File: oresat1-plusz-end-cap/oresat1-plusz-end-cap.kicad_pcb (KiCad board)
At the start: 4 copper layers, 105.6 x 105.6 mm, 55 parts, among them J1 M55-7011242R, J2 U.FL-R-SMA, U1 RM3100, U2 RM3100

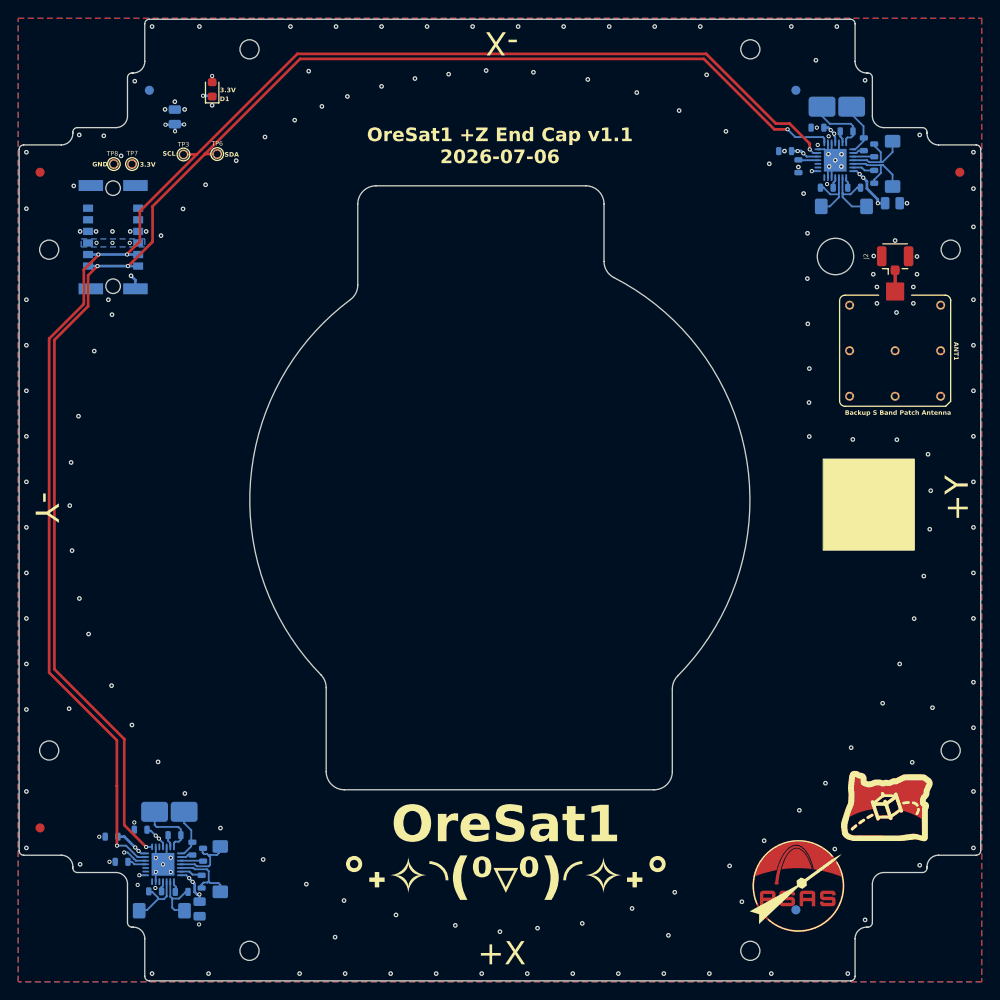
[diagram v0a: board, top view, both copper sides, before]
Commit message: Changes to layout
Aligned some magnetometer coils to align with axis of oresat 1
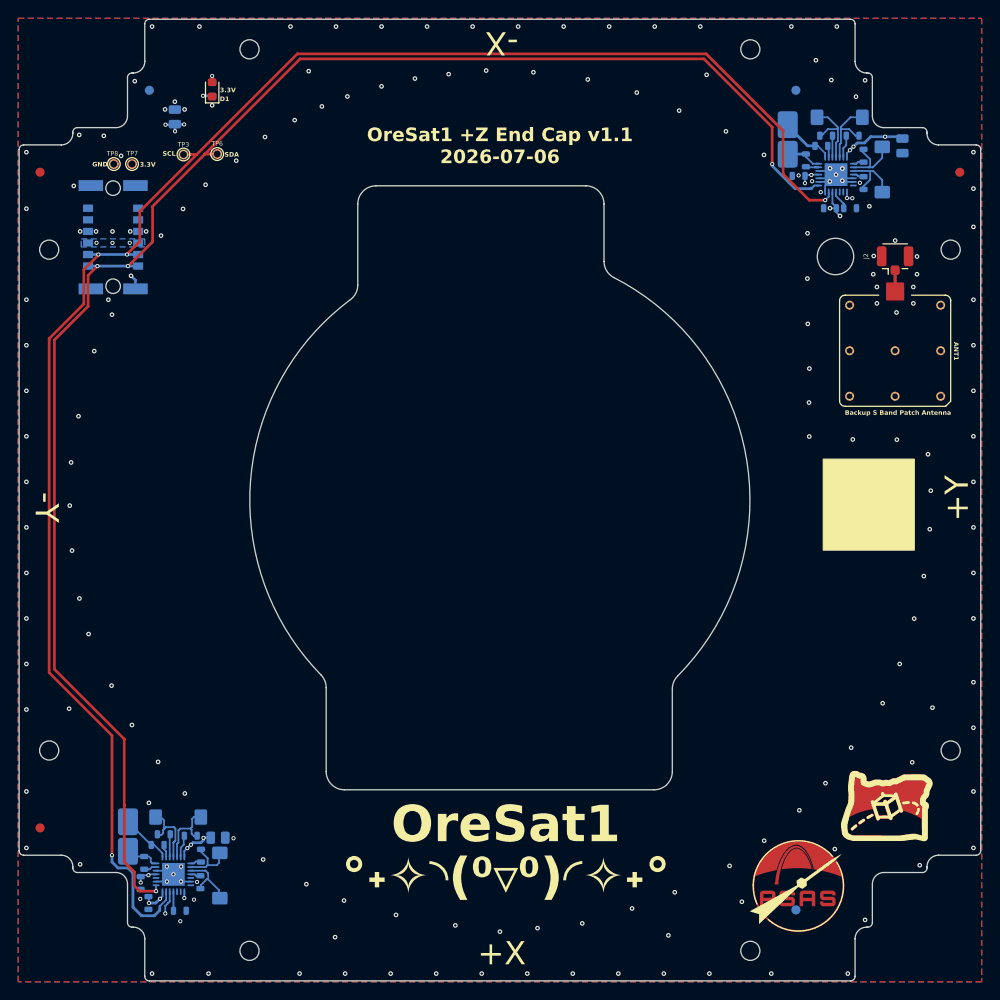
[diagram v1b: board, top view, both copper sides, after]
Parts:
- moved R9 8.36 mm to (113.3, 150.1), turned to 180 degrees
- moved C5 8.33 mm to (109.9, 149.2), turned to -90 degrees
- moved C3 8.07 mm to (117.5, 142.1), turned to 0 degrees
- moved C1 7.98 mm to (184.8, 73.0)
- moved L3 7.74 mm to (185.8, 63.0), turned to 180 degrees
- moved L7 7.45 mm to (117.7, 146.2), turned to 90 degrees
- moved L8 7.35 mm to (113.2, 139.8), turned to 180 degrees
- moved R8 7.31 mm to (186.9, 73.0), turned to 180 degrees
- moved L5 6.49 mm to (180.1, 65.4), turned to 90 degrees
- moved C2 6.40 mm to (192.7, 66.1), turned to -90 degrees
- moved C7 5.85 mm to (109.0, 147.1), turned to -90 degrees
- moved L4 5.84 mm to (190.5, 68.7), turned to 90 degrees
- moved C4 5.69 mm to (181.3, 69.4)
- moved R4 5.51 mm to (184.3, 65.0), turned to 0 degrees
- moved R6 5.49 mm to (182.1, 67.7), turned to -90 degrees
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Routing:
- net /MAG-SCL: track 172.7 -> 189.5 mm
- net /MAG-SDA: track 169.8 -> 180.0 mm
- net Net-(U2-ZINP): track 7.27 -> 4.44 mm
- net GND: track 18.2 -> 15.3 mm, vias 183 -> 178
- net Net-(U1-ZINP): track 6.63 -> 4.15 mm
- net +3.3v: track 30.2 -> 31.8 mm, vias 24 -> 27
- net Net-(U2-ZDRVP): track 1.30 -> 1.84 mm

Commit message: routine push
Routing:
- net Net-(U1-ZINP): track 4.15 -> 4.67 mm
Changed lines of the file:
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@@
+	)
+	(segment
+		(start 110.745 146.89)
+		(end 111.9225 146.89)
+		(width 0.2)
+		(layer "B.Cu")
+		(net "GND")
 	)
 	(segment
@@
 	)
 	(segment
-		(start 110.745 146.89)
-		(end 111.9225 146.89)
-		(width 0.2)
-		(layer "B.Cu")
-		(net "GND")
-	)
-	(segment
 		(start 114.55 146.9)
 		(end 113.4825 146.9)
@@
 	)
 	(segment
+		(start 110.3125 144.9)
+		(end 110.1525 144.74)
+		(width 0.2)
+		(layer "B.Cu")
+		(net "Net-(U1-ZINP)")
+	)
+	(segment
 		(start 109.44 144.14)
 		(end 108.215 144.14)
@@
 	)
 	(segment
+		(start 110.735 144.9)
+		(end 110.3125 144.9)
+		(width 0.2)
+		(layer "B.Cu")
+		(net "Net-(U1-ZINP)")
+	)
+	(segment
+		(start 109.9525 144.14)
+		(end 109.44 144.14)
+		(width 0.2)
+		(layer "B.Cu")
+		(net "Net-(U1-ZINP)")
+	)
+	(segment
 		(start 110.1525 144.34)
 		(end 109.9525 144.14)
@@
 	)
 	(segment
-		(start 110.3125 144.9)
-		(end 110.1525 144.74)
-		(width 0.2)
-		(layer "B.Cu")
-		(net "Net-(U1-ZINP)")
-	)
-	(segment
 		(start 108.215 144.14)
 		(end 107.65 143.575)
 		(width 0.2)
 		(layer "B.Cu")
-		(net "Net-(U1-ZINP)")
-	)
-	(segment
-		(start 110.735 144.9)
-		(end 110.3125 144.9)
-		(width 0.2)
-		(layer "B.Cu")

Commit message: routine push
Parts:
- added R16: 121, oresat-passives:0603-C-NOSILK, B.Cu at (117.8, 151.2)
- added R17: 121, oresat-passives:0603-C-NOSILK, B.Cu at (117.8, 150.1)
- added R18: 121, oresat-passives:0603-C-NOSILK, B.Cu at (115.6, 151.2)
- added R19: 121, oresat-passives:0603-C-NOSILK, B.Cu at (115.6, 150.1)
- moved R7 0.05 mm to (183.8, 66.1)
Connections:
- U1 pad 28: +3.3v -> Net-(U1-MISO/SA1)
- U1 pad 3: GND -> Net-(U1-SSN/SA0)
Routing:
- net Net-(U1-SSN/SA0): track 0.00 -> 9.65 mm, vias 0 -> 2
- net Net-(U1-MISO/SA1): track 0.00 -> 7.85 mm, vias 0 -> 2
- net +3.3v: track 31.8 -> 32.7 mm, vias 27 -> 24
- net GND: vias 178 -> 181

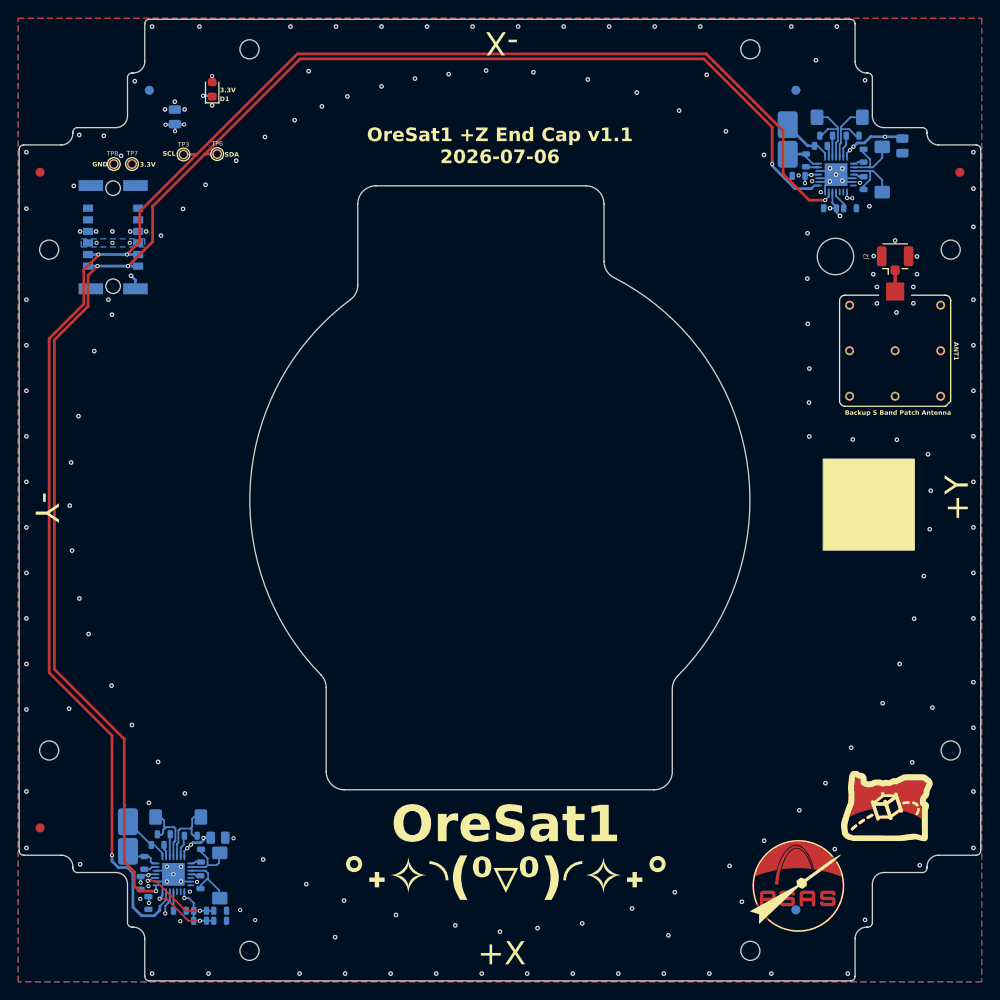
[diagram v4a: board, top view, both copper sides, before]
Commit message: Added releases, cleaned up PNI inductors, fixed ERCs and DRCs.
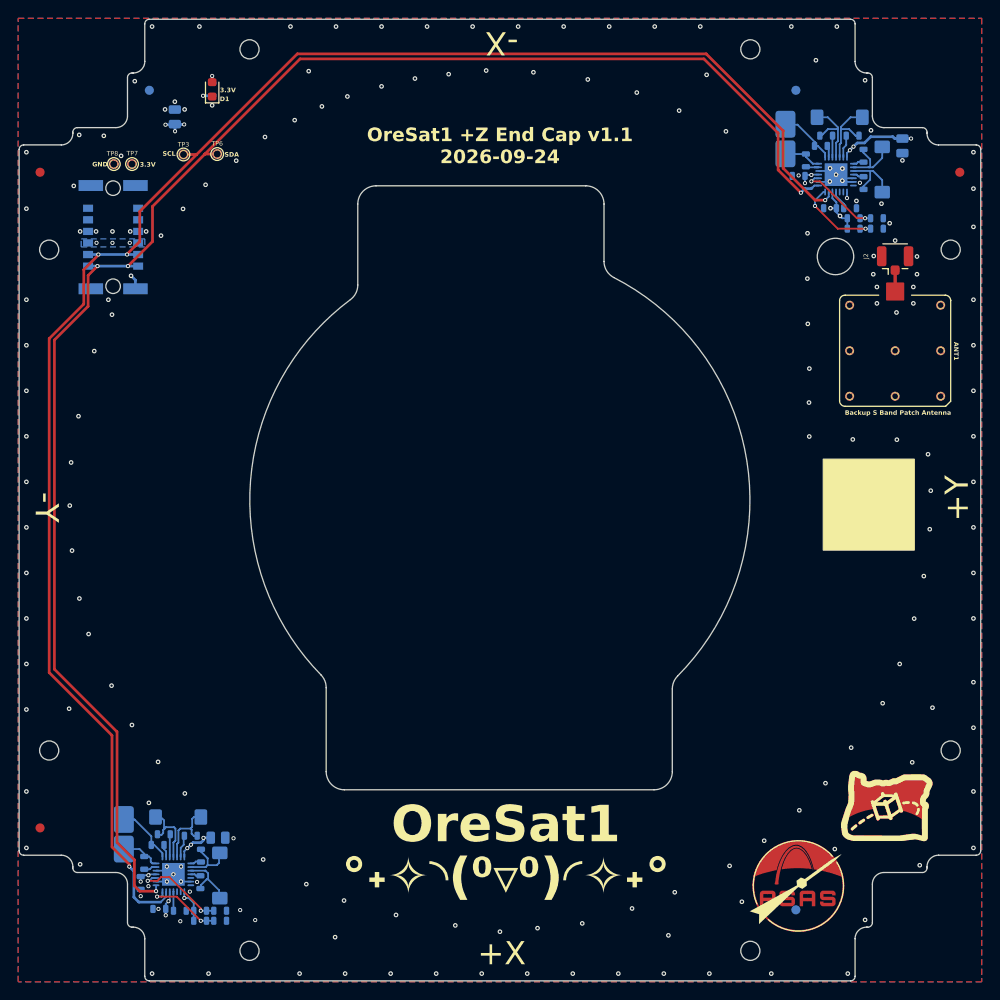
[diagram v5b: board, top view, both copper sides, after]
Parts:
- added R20: 121, oresat-passives:0603-C-NOSILK, B.Cu at (187.3, 75.2)
- added R21: 121, oresat-passives:0603-C-NOSILK, B.Cu at (189.9, 75.2)
- added R22: 121, oresat-passives:0603-C-NOSILK, B.Cu at (187.3, 74.0)
- added R23: 121, oresat-passives:0603-C-NOSILK, B.Cu at (189.9, 74.0)
- moved C5 1.36 mm to (111.1, 149.9), turned to 180 degrees
- moved L9 0.51 mm to (107.2, 141.7)
- moved L5 0.25 mm to (179.8, 65.3)
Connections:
- U2 pad 28: GND -> Net-(U2-MISO/SA1)
- U2 pad 3: GND -> Net-(U2-SSN/SA0)
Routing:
- net Net-(U2-MISO/SA1): track 0.00 -> 9.53 mm, vias 0 -> 2
- net Net-(U2-SSN/SA0): track 0.00 -> 9.37 mm, vias 0 -> 2
- net /MAG-SCL: track 189.4 -> 186.0 mm
- net GND: track 15.3 -> 13.1 mm, vias 181 -> 183
- net +3.3v: track 32.7 -> 34.5 mm, vias 24 -> 23
- net Net-(U1-ZINN): track 5.64 -> 6.75 mm
- net Net-(U1-ZINP): track 4.67 -> 5.40 mm
- net Net-(U1-MISO/SA1): track 7.85 -> 8.40 mm

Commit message: Updated paste for PNI sensors, better layout, polishing.
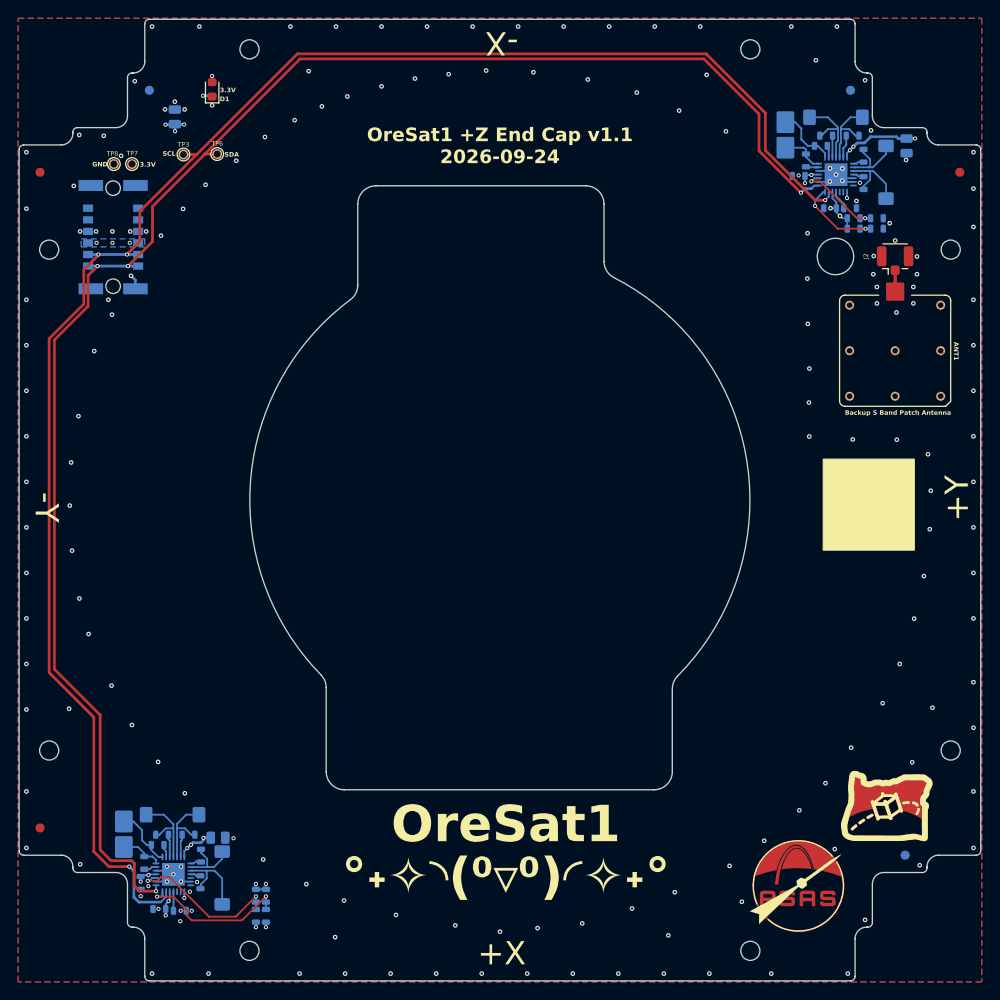
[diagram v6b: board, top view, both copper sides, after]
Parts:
- U1, U2: footprint oresat-misc:RM3100-MagI2C -> oresat-ics:U-PNI-RM3100-IC
- moved FID106 13.4 mm to (193.0, 144.0)
- moved R18 7.73 mm to (122.8, 148.4), turned to -90 degrees
- moved R19 6.34 mm to (121.7, 148.4), turned to -90 degrees
- moved FID104 6.00 mm to (187.0, 60.0)
- moved R16 5.06 mm to (122.8, 150.7), turned to -90 degrees
- moved R17 3.96 mm to (121.7, 150.7), turned to -90 degrees
- moved L8 0.67 mm to (112.5, 139.6), turned to 0 degrees
- moved L4 0.52 mm to (190.9, 69.0), turned to -90 degrees
- moved C2 0.45 mm to (193.2, 66.1)
- moved L5 0.45 mm to (179.8, 64.9)
- moved L3 0.41 mm to (185.4, 63.0), turned to 0 degrees
- moved L7 0.37 mm to (118.0, 146.5), turned to -90 degrees
- moved R13 0.27 mm to (114.3, 141.8)
- moved R12 0.20 mm to (111.4, 141.8)
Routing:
- net Net-(U1-MISO/SA1): track 8.40 -> 17.0 mm
- net Net-(U1-SSN/SA0): track 10.1 -> 17.2 mm
- net Net-(U1-XINN): track 6.73 -> 8.91 mm
- net Net-(U1-YINP): track 7.74 -> 9.09 mm
- net /MAG-SCL: track 186.0 -> 187.4 mm
- net /MAG-SDA: track 180.2 -> 181.6 mm
- net Net-(U2-XINN): track 7.09 -> 7.97 mm
- net Net-(U1-YINN): track 7.82 -> 8.71 mm
- net Net-(U2-YINP): track 8.42 -> 9.24 mm
- net Net-(U2-ZINN): track 6.09 -> 6.87 mm
- net Net-(U2-ZINP): track 4.28 -> 4.85 mm
- net +3.3v: track 34.5 -> 34.0 mm, vias 23 -> 25
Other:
- board text added: "+X->"
- board text added: "+Y->"

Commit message: Polishing layout, mostly stiching
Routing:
- net GND: vias 183 -> 198
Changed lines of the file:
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@@
 	)
 	(via
+		(at 194.7 71.7)
+		(size 0.4572)
+		(drill 0.254)
+		(layers "F.Cu" "B.Cu")
+		(free yes)
+		(net "GND")
+	)
+	(via
 		(at 96.5 66.8)
 		(size 0.508)
@@
 	)
 	(via
+		(at 182.1 72)
+		(size 0.4572)
+		(drill 0.254)
+		(layers "F.Cu" "B.Cu")
+		(free yes)
+		(net "GND")
+	)
+	(via
 		(at 105 65)
 		(size 0.508)
@@
 	)
 	(via
+		(at 181.2 61.9)
+		(size 0.4572)
+		(drill 0.254)
+		(layers "F.Cu" "B.Cu")
+		(free yes)
+		(net "GND")
+	)
+	(via
+		(at 108.7 151.3)
+		(size 0.4572)
+		(drill 0.254)
+		(layers "F.Cu" "B.Cu")
+		(free yes)
+		(net "GND")
+	)
+	(via
 		(at 186.1 68.6)
 		(size 0.508)
@@
 	)
 	(via
+		(at 102.5 136.5)
+		(size 0.4572)
+		(drill 0.254)
+		(layers "F.Cu" "B.Cu")
+		(free yes)
+		(net "GND")
+	)
+	(via
 		(at 156.5 157)
 		(size 0.508)
@@
 	)
 	(via
+		(at 187.4 86.3)
+		(size 0.4572)
+		(drill 0.254)
+		(layers "F.Cu" "B.Cu")
+		(free yes)
+		(net "GND")
+	)
+	(via
 		(at 193.99 118.02)
 		(size 0.508)
@@
 	)
 	(via
+		(at 196.7 86.4)
+		(size 0.4572)
+		(drill 0.254)
+		(layers "F.Cu" "B.Cu")
+		(free yes)
+		(net "GND")
+	)
+	(via
 		(at 113.4 151.25)
 		(size 0.4572)
@@
 	)
 	(via
+		(at 187.5 90.9)
+		(size 0.4572)
+		(drill 0.254)
+		(layers "F.Cu" "B.Cu")
+		(free yes)
+		(net "GND")
+	)
+	(via
 		(at 182.47 98.02)
 		(size 0.508)
@@
 	)
 	(via
+		(at 119.4 147.7)
+		(size 0.4572)
+		(drill 0.254)
+		(layers "F.Cu" "B.Cu")
+		(free yes)
+		(net "GND")
+	)
+	(via
 		(at 152.63 152.01)
 		(size 0.508)
@@
 	)
 	(via
+		(at 191.9 86.2)
+		(size 0.4572)
+		(drill 0.254)
+		(layers "F.Cu" "B.Cu")
+		(free yes)
+		(net "GND")
+	)
+	(via
 		(at 189.9 83.4)
 		(size 0.508)
@@
 	)
 	(via
+		(at 196.5 90.9)
+		(size 0.4572)
+		(drill 0.254)
+		(layers "F.Cu" "B.Cu")
+		(free yes)
+		(net "GND")
+	)
+	(via
 		(at 143.6 151.71)
 		(size 0.508)
@@
 	)
 	(via
+		(at 192 91)
+		(size 0.4572)
+		(drill 0.254)
+		(layers "F.Cu" "B.Cu")
+		(free yes)
+		(net "GND")
+	)
+	(via
 		(at 101.19 127.91)
 		(size 0.508)
@@
 	)
 	(via
+		(at 107.9 137.8)
+		(size 0.4572)
+		(drill 0.254)
+		(layers "F.Cu" "B.Cu")
+		(free yes)
+		(net "GND")
+	)
+	(via
+		(at 105.4 142.9)
+		(size 0.4572)
+		(drill 0.254)
+		(layers "F.Cu" "B.Cu")
+		(free yes)
+		(net "GND")
+	)
+	(via
 		(at 195.05 113.35)
 		(size 0.508)
@@
 		(net "GND")
 	)
+	(via
+		(at 116.9 147.5)
+		(size 0.4572)
+		(drill 0.254)
+		(layers "F.Cu" "B.Cu")
+		(free yes)
+		(net "GND")
+	)
